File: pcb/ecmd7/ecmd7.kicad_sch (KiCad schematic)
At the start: 90 parts, among them J1 PMOD_SPI_ENC, J2 PMOD_ADC_MPIO, J3 PMOD_DRV, J4 Conn_01x02_Socket, J5 Encoder, J6 12V, J7 RS422/BISS-C, J8 5V, Q1 IRFS3806, Q11 MMBT3904, Q12 MMBT3904, Q2 IRFS3806, Q3 IRFS3806, Q4 IRFS3806, Q5 IRFS3806, Q6 IRFS3806, U1 TMC6200-TA

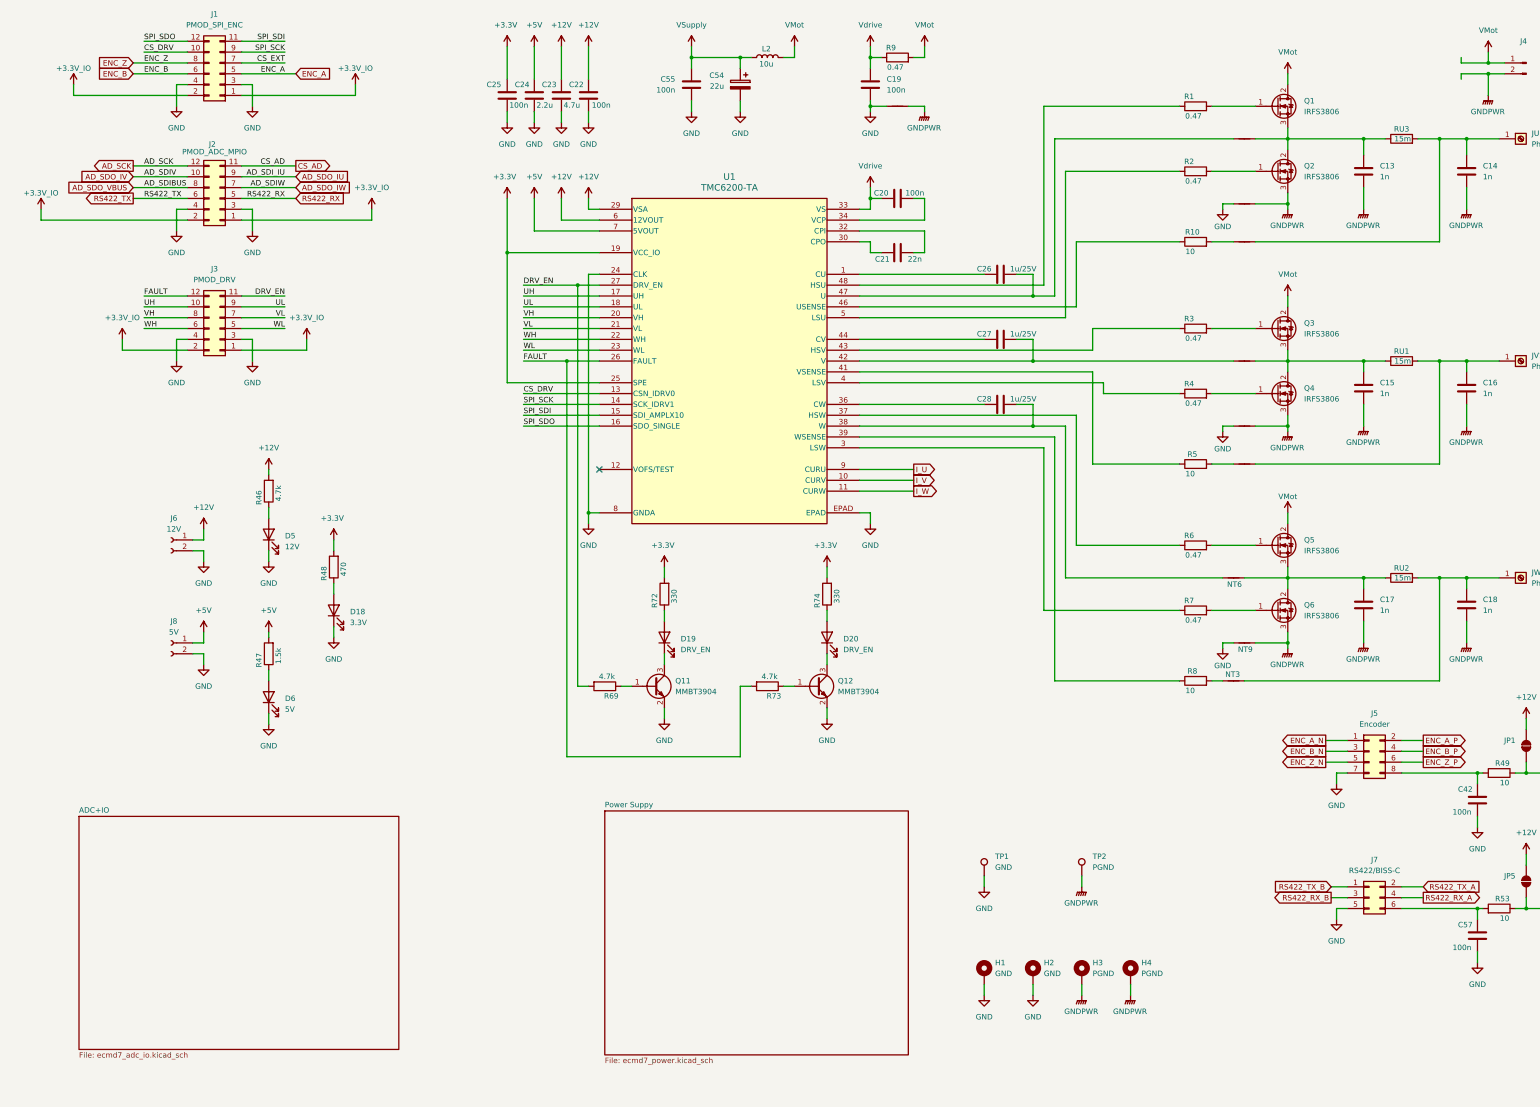
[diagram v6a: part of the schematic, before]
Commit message: WIP: Update symbols, fix ERC errors
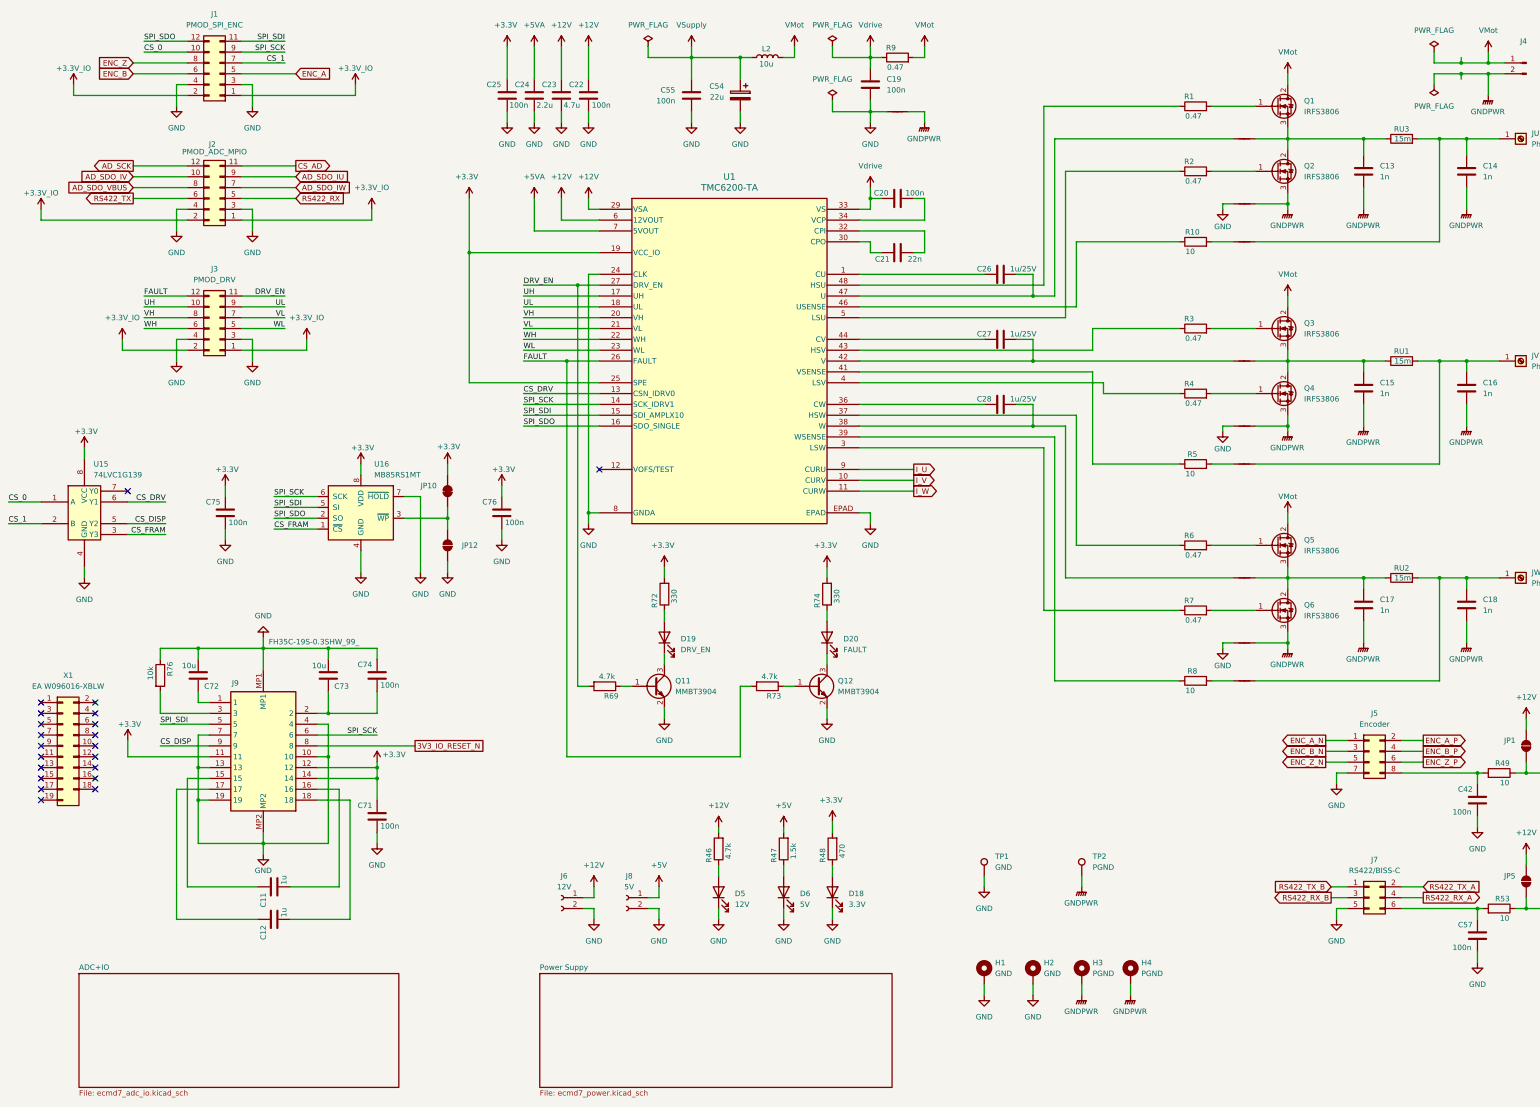
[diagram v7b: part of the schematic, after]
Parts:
- added C11, C12: 1u, Capacitor_SMD:C_0805_2012Metric, symbol Device:C
- added C71, C74, C75, C76: 100n, Capacitor_SMD:C_0805_2012Metric, symbol Device:C
- added C72, C73: 10u, Capacitor_SMD:C_0805_2012Metric, symbol Device:C
- added J9: FH35C-19S-0.3SHW_99_, SSTA:FH35C19S03SHW99, symbol SSTA:FH35C-19S-0.3SHW_99_
- added JP10: SolderJumper_2_Bridged, Jumper:SolderJumper-2_P1.3mm_Bridged_RoundedPad1.0x1.5mm, symbol Jumper:SolderJumper_2_Bridged
- added JP12: SolderJumper_2_Open, Jumper:SolderJumper-2_P1.3mm_Open_RoundedPad1.0x1.5mm, symbol Jumper:SolderJumper_2_Open
- added R76: 10k, Resistor_SMD:R_0805_2012Metric, symbol Device:R
- added U15: 74LVC1G139, Package_SO:SSOP-8_2.95x2.8mm_P0.65mm, symbol 74xGxx:74LVC1G139
- added U16: MB85RS1MT, Package_SO:SOP-8_3.76x4.96mm_P1.27mm, symbol Memory_NVRAM:MB85RS1MT
- added X1: EA W096016-XBLW, symbol Connector_Generic:Conn_2Rows-19Pins
- D20: value DRV_EN -> FAULT
- J6, J8: footprint Connector_PinHeader_2.00mm:PinHeader_1x02_P2.00mm_Vertical -> Connector_PinHeader_2.54mm:PinHeader_1x02_P2.54mm_Vertical
- NTGU1: renamed from NT7; footprint NetTie:NetTie-2_SMD_Pad2.0mm -> NetTie:NetTie-2_SMD_Pad0.5mm
- NTGV1: renamed from NT8; footprint NetTie:NetTie-2_SMD_Pad2.0mm -> NetTie:NetTie-2_SMD_Pad0.5mm
- NTGW1: renamed from NT9; footprint NetTie:NetTie-2_SMD_Pad2.0mm -> NetTie:NetTie-2_SMD_Pad0.5mm
- U1: footprint sst_footprints:eTQFP48_9x9_TRI -> SSTA:eTQFP48_9x9_TRI; symbol ssta_symbols:TMC6200-TA -> SSTA:TMC6200-TA
- renumbered NT10 to NTP2G1, NT4 to NTPU1, NT5 to NTPV1, NT6 to NTPW1, NT1 to NTSU1, NT2 to NTSV1, NT3 to NTSW1
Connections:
- net +3.3V: now also C71.1, C75.1, C76.1, J9.11, J9.12, J9.14, JP10.2 (B), U15.8 (VCC), U16.8 (VDD)
- net +5V: no longer C24.1, U1.7 (5VOUT)
- net CS_DRV: now also U15.6 (Y1); no longer J1.10 (Pin_10)
- net GND: now also C71.2, C72.2, C73.2, C74.1, C75.2, C76.2, J9.10, J9.13, J9.19, J9.4, J9.7, J9.MP1, J9.MP2, JP12.1 (A), R76.1, U15.4 (GND), U16.4 (GND), U16.7 (~{HOLD})
- net SPI_SCK: now also J9.6, U16.6 (SCK)
- net SPI_SDI: now also J9.5, U16.5 (SI)
- net SPI_SDO: now also U16.2 (SO)
- net CS_EXT renamed CS_1
- net CS_1: now also U15.2 (B)
- new net: C11.1, J9.15
- new net: C11.2, J9.16
- new net: C12.1, J9.17
- new net: C12.2, J9.18
- new net: JP10.1 (A), JP12.2 (B), U16.3 (~{WP})
- new net: C73.1, C74.2, J9.2
- new net: J9.3, R76.2
- new net: C72.1, J9.1
- new net +5VA: C24.1, U1.7 (5VOUT)
- new net 3V3_IO_RESET_N: J9.8
- new net CS_0: J1.10 (Pin_10), U15.1 (A)
- new net CS_DISP: J9.9, U15.5 (Y2)
- new net CS_FRAM: U15.3 (Y3), U16.1 (~{CS})
- no-connect marks 1 -> 21
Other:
- moved on the sheet: C54, C55, D18, D5, D6, J6, J8, R46, R47, R48

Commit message: WIP: Power stage and ADC routing
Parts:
- added D21: SMAJ60A, Diode_SMD:D_SMA, symbol Diode:SMAJ60A
- added J10: SPI Ext., Connector_PinSocket_2.54mm:PinSocket_1x06_P2.54mm_Vertical, symbol Connector:Conn_01x06_Socket
- added NTPV2, NTPW3: NetTie_2, NetTie:NetTie-2_SMD_Pad0.5mm, symbol Device:NetTie_2
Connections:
- net +3.3V: now also J10.1 (Pin_1)
- net CS_FRAM: now also J10.6 (Pin_6)
- net GND: now also J10.2 (Pin_2), NTPV2.2
- net GNDPWR: now also D21.2 (A2), NTPW3.2
- net SPI_SCK: now also J10.3 (Pin_3)
- net SPI_SDI: now also J10.4 (Pin_4)
- net SPI_SDO: now also J10.5 (Pin_5)
- net VMot: now also D21.1 (A1)
- net CS_EXT: now reaches U15.7 (Y0)
- new net I_REF: NTPV2.1
- new net VMOT_REF: NTPW3.1
- no-connect marks 21 -> 20
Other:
- moved on the sheet: C11, C12, C13, C14, C15, C16, C17, C18, C20, C21, C26, C27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
